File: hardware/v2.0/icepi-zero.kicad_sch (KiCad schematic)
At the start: 25 parts, among them J1 Conn_02x20_Counter_Clockwise, SW1 SW_Push, SW2 SW_Push, U1 ECP5U-25F-CABGA256, Y1 SG-8018CG 50.000000MHz

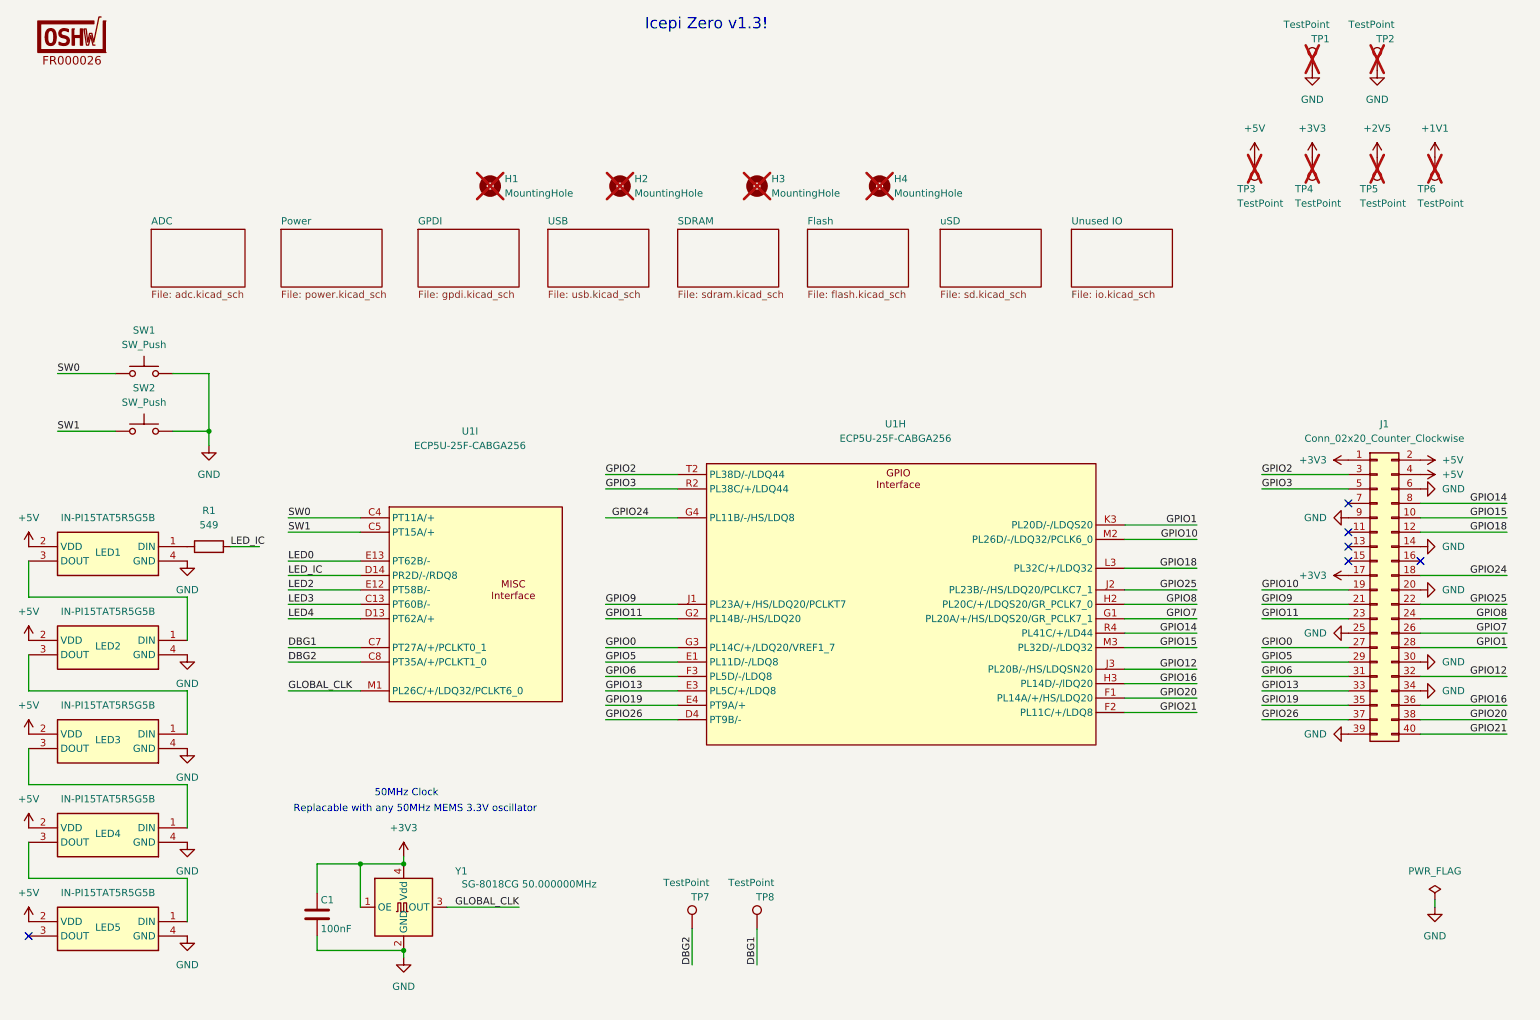
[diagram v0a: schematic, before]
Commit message: ADC driver adjustment
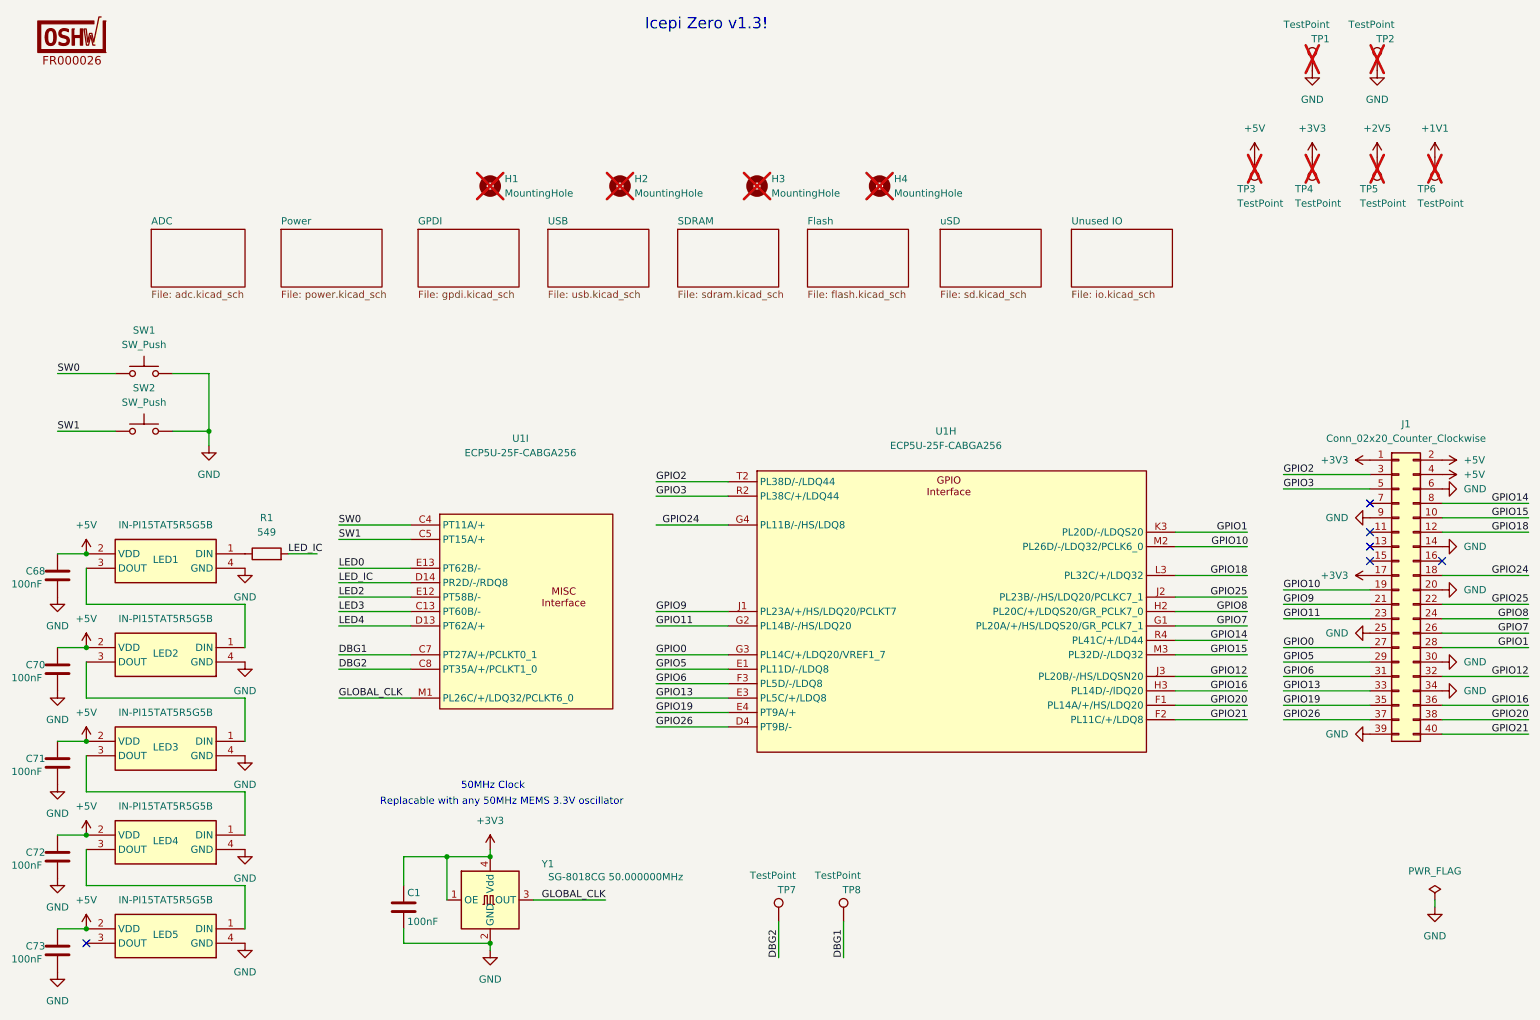
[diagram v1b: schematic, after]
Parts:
- added C68, C70, C71, C72, C73: 100nF, Capacitor_SMD:C_0402_1005Metric, symbol Device:C
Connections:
- net +5V: now also C68.1, C70.1, C71.1, C72.1, C73.1
- net GND: now also C68.2, C70.2, C71.2, C72.2, C73.2
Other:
- moved on the sheet: C1, J1, LED1, LED2, LED3, LED4, LED5, R1, TP7, TP8, U1H, U1I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

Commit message: ADC SPI
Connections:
- removed net LED0: U1.E13 (PT62B/-)
- removed net LED2: U1.E12 (PT58B/-)
- removed net LED3: U1.C13 (PT60B/-)
- removed net LED4: U1.D13 (PT62A/+)
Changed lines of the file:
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@@
-	(wire
-		(pts
-			(xy 71.12 114.3) (xy 83.82 114.3)
-		)
-		(stroke
-			(width 0)
-			(type default)
-		)
-	)
 	(wire
 		(pts
@@
 	(wire
 		(pts
-			(xy 71.12 121.92) (xy 83.82 121.92)
-		)
-		(stroke
-			(width 0)
-			(type default)
-		)
-	)
-	(wire
-		(pts
 			(xy 127 106.68) (xy 139.7 106.68)
 		)
@@
 	(wire
 		(pts
-			(xy 71.12 119.38) (xy 83.82 119.38)
-		)
-		(stroke
-			(width 0)
-			(type default)
-		)
-	)
-	(wire
-		(pts
 			(xy 21.59 144.78) (xy 26.67 144.78)
 		)
@@
 		(pts
 			(xy 148.59 176.53) (xy 148.59 182.88)
-		)
-		(stroke
-			(width 0)
-			(type default)
-		)
-	)
-	(wire
-		(pts
-			(xy 71.12 124.46) (xy 83.82 124.46)
 		)
 		(stroke
@@
 		)
 	)
-	(label "LED4"
-		(at 71.12 124.46 0)
-		(effects
-			(font
-				(size 1.27 1.27)
-			)
-			(justify left bottom)
-		)
-	)
 	(label "GPIO11"
 		(at 127 124.46 0)
@@
 		)
 	)
-	(label "LED2"
-		(at 71.12 119.38 0)
-		(effects
-			(font
-				(size 1.27 1.27)
-			)
-			(justify left bottom)
-		)
-	)
 	(label "GPIO3"
 		(at 237.49 100.33 0)
@@
 		)
 	)
-	(label "LED3"
-		(at 71.12 121.92 0)
-		(effects
-			(font
-				(size 1.27 1.27)
-			)
-			(justify left bottom)
-		)
-	)
 	(label "DBG1"
 		(at 160.02 182.88 90)
@@
 		(effects
 			(font
-				(size 1.27 1.27)
-			)
-			(justify left bottom)
-		)
-	)
-	(label "LED0"
-		(at 71.12 114.3 0)
-		(effects
-			(font

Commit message: ADC SPI SDO
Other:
- note added: "Icepi Zero v2.0!"
- note removed: "Icepi Zero v1.3!"
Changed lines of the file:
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@@
 		(comment 9 "OSHWA FR000026")
 	)
-	(text "Icepi Zero v1.3!"
+	(text "Icepi Zero v2.0!"
 		(exclude_from_sim no)
 		(at 135.89 18.542 0)
@@
 	(wire
 		(pts
-			(xy 264.16 173.99) (xy 264.16 172.72)
+			(xy 171.45 176.53) (xy 171.45 175.26)
 		)
 		(stroke
@@
 	(symbol
 		(lib_id "power:GND")
-		(at 264.16 173.99 0)
+		(at 171.45 176.53 0)
 		(unit 1)
 		(exclude_from_sim no)
@@
 		(fields_autoplaced yes)
 		(property "Reference" "#PWR021"
-			(at 264.16 180.34 0)
+			(at 171.45 182.88 0)
 			(effects
 				(font
@@
 		)
 		(property "Value" "GND"
-			(at 264.16 179.07 0)
+			(at 171.45 181.61 0)
 			(effects
 				(font
@@
 		)
 		(property "Footprint" ""
-			(at 264.16 173.99 0)
+			(at 171.45 176.53 0)
 			(effects
 				(font
@@
 		)
 		(property "Datasheet" ""
-			(at 264.16 173.99 0)
+			(at 171.45 176.53 0)
 			(effects
 				(font
@@
 		)
 		(property "Description" "Power symbol creates a global label with name \"GND\" , ground"
-			(at 264.16 173.99 0)
+			(at 171.45 176.53 0)
 			(effects
 				(font
@@
 	(symbol
 		(lib_id "power:PWR_FLAG")
-		(at 264.16 172.72 0)
+		(at 171.45 175.26 0)
 		(unit 1)
 		(exclude_from_sim no)
@@
 		(fields_autoplaced yes)
 		(property "Reference" "#FLG01"
-			(at 264.16 170.815 0)
+			(at 171.45 173.355 0)
 			(effects
 				(font
@@
 		)
 		(property "Value" "PWR_FLAG"
-			(at 264.16 167.64 0)
+			(at 171.45 170.18 0)
 			(effects
 				(font
@@
 		)
 		(property "Footprint" ""
-			(at 264.16 172.72 0)
+			(at 171.45 175.26 0)
 			(effects
 				(font
@@
 		)
 		(property "Datasheet" "~"
-			(at 264.16 172.72 0)
+			(at 171.45 175.26 0)
 			(effects
 				(font
@@
 		)
 		(property "Description" "Special symbol for telling ERC where power comes from"
-			(at 264.16 172.72 0)
+			(at 171.45 175.26 0)
 			(effects
 				(font

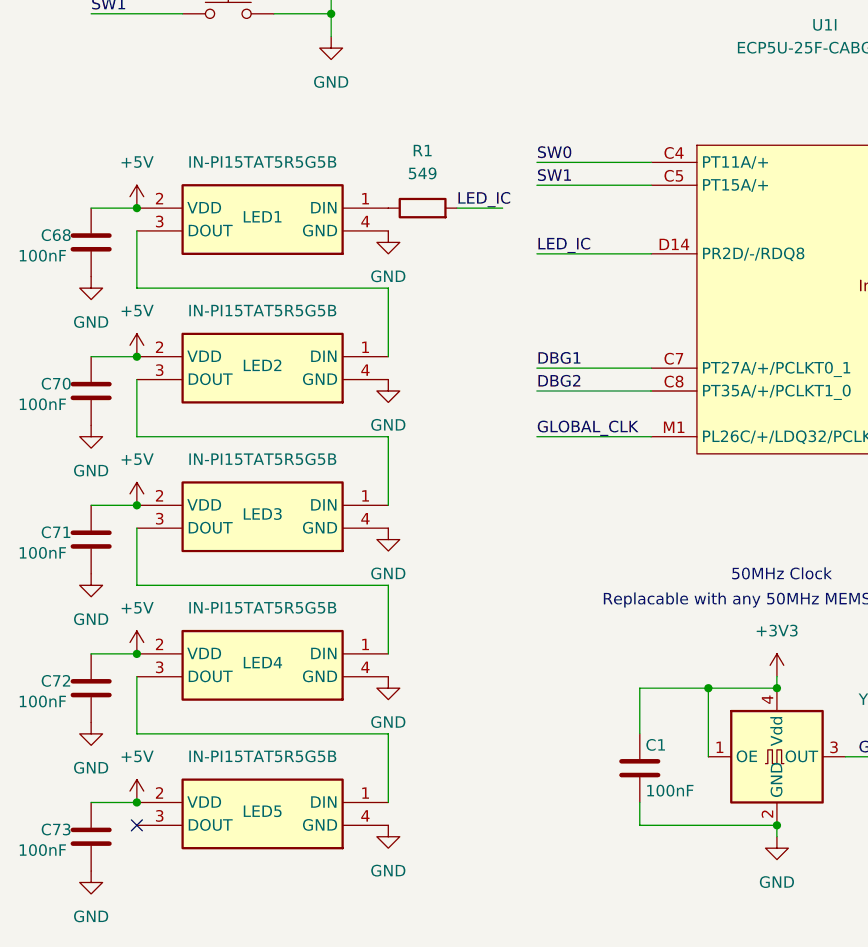
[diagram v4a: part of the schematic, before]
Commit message: BOM fields unification for PCBWay requirements
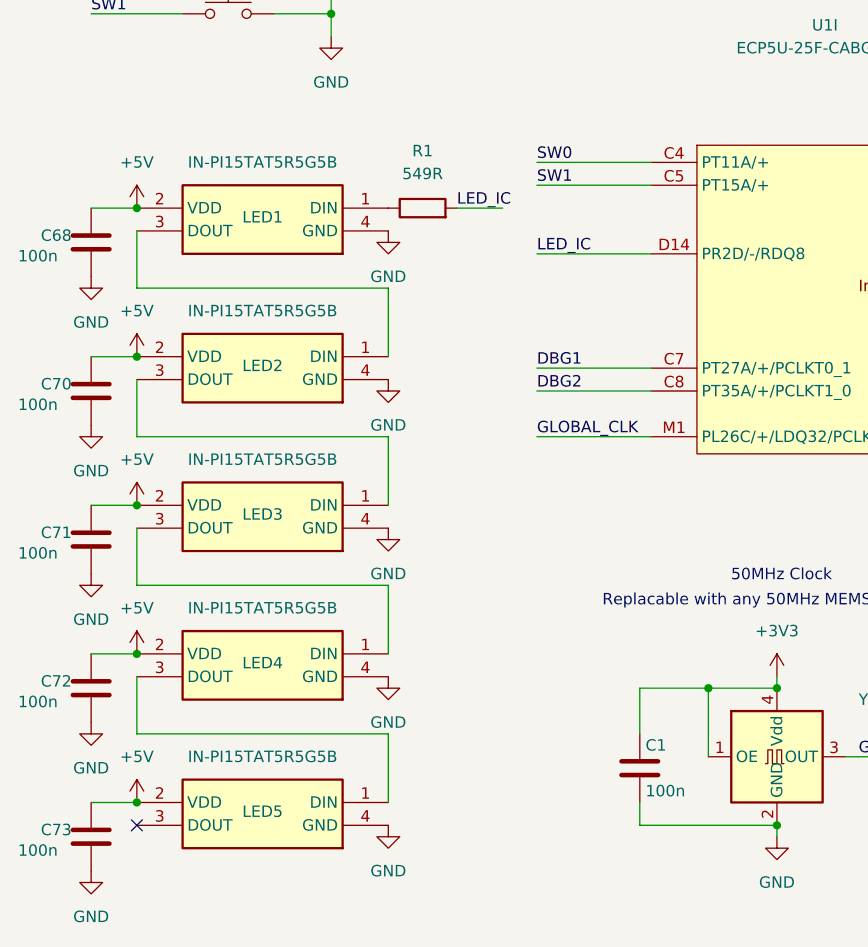
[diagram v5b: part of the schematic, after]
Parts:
- C1, C68, C70, C71, C72, C73: value 100nF -> 100n; MANUFACTURER (none) -> Samsung Electro-Mechanics; MANUFACTURER_PART_NUMBER (none) -> CL05B104KB54PNC
- LED1, LED2, LED3, LED4, LED5: MANUFACTURER (none) -> Inolux; MANUFACTURER_PART_NUMBER (none) -> IN-PI15TAT5R5G5B
- R1: value 549 -> 549R; MANUFACTURER (none) -> UNI-ROYAL; MANUFACTURER_PART_NUMBER (none) -> 0402WGF5490TCE
- SW1, SW2: MANUFACTURER (none) -> XUNPU; MANUFACTURER_PART_NUMBER (none) -> TS-1088-AR02016
- U1: MANUFACTURER (none) -> Lattice; MANUFACTURER_PART_NUMBER (none) -> LFE5U-25F-6BG256C
- Y1: MANUFACTURER (none) -> EPSON; MANUFACTURER_PART_NUMBER (none) -> SG-8018CG 50.000000MHz TJHSA

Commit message: Repo links update
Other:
- title: Icepi Zero -> GammaPi Zero
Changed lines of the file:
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@@
 	(paper "A4")
 	(title_block
-		(title "Icepi Zero")
-		(date "2026-01-17")
-		(rev "v2.1")
+		(title "GammaPi Zero")
+		(date "2026-01-25")
+		(rev "v2.3.2")
 		(company "Vadym Vikulin, Chengyin Yao (cheyao)")
-		(comment 1 "https://github.com/vikulin/icepi-zero")
+		(comment 1 "https://github.com/vikulin/gammapi-zero")
 		(comment 2 "License: Solderpad")
 		(comment 9 "OSHWA FR000026")

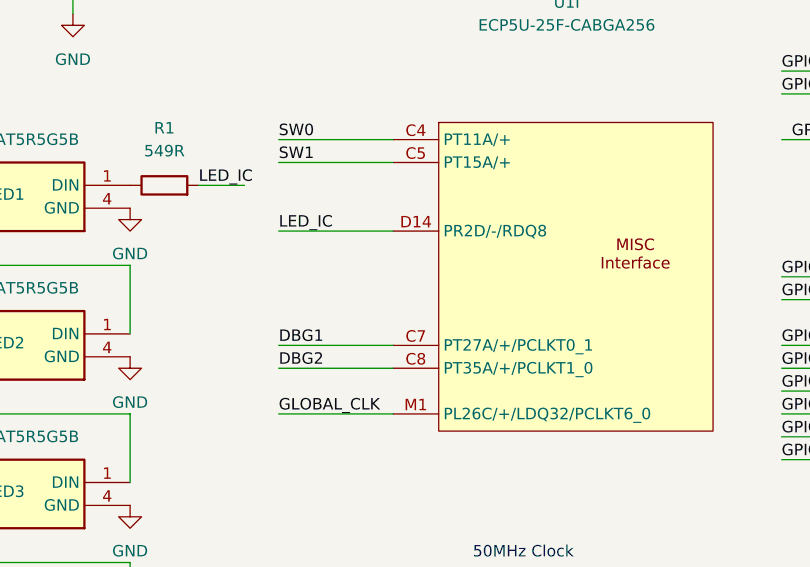
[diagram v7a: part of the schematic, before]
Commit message: Extra CS for SPI
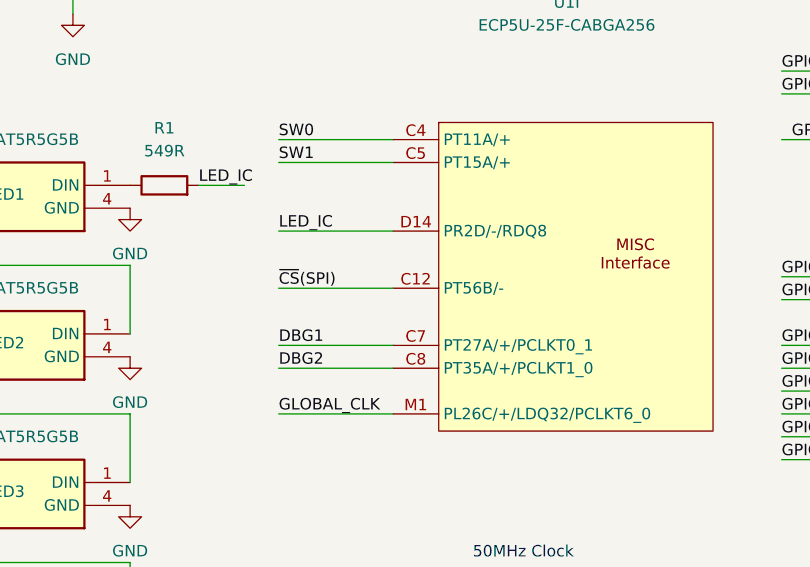
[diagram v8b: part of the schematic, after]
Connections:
- new net ~{CS}(SPI): U1.C12 (PT56B/-)
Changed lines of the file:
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@@
 	(wire
 		(pts
+			(xy 71.12 123.19) (xy 83.82 123.19)
+		)
+		(stroke
+			(width 0)
+			(type default)
+		)
+	)
+	(wire
+		(pts
 			(xy 171.45 176.53) (xy 171.45 175.26)
 		)
@@
 		)
 	)
+	(label "~{CS}(SPI)"
+		(at 71.12 123.19 0)
+		(effects
+			(font
+				(size 1.27 1.27)
+			)
+			(justify left bottom)
+		)
+	)
 	(label "GPIO7"
 		(at 280.67 125.73 180)
@@
 		(pin "C7"
 		)
-		(pin "C11"
-		)
 		(pin "C12"
 		)
@@
 		(pin "N6"
 		)
+		(pin "C11"
+		)
 		(instances
 			(project ""
@@
 		(pin "E10"
 		)
-		(pin "C11"
-		)
 		(pin "L3"
 		)
@@
 		(pin "N6"
 		)
+		(pin "C11"
+		)
 		(instances
